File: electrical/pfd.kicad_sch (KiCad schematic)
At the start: 8 parts

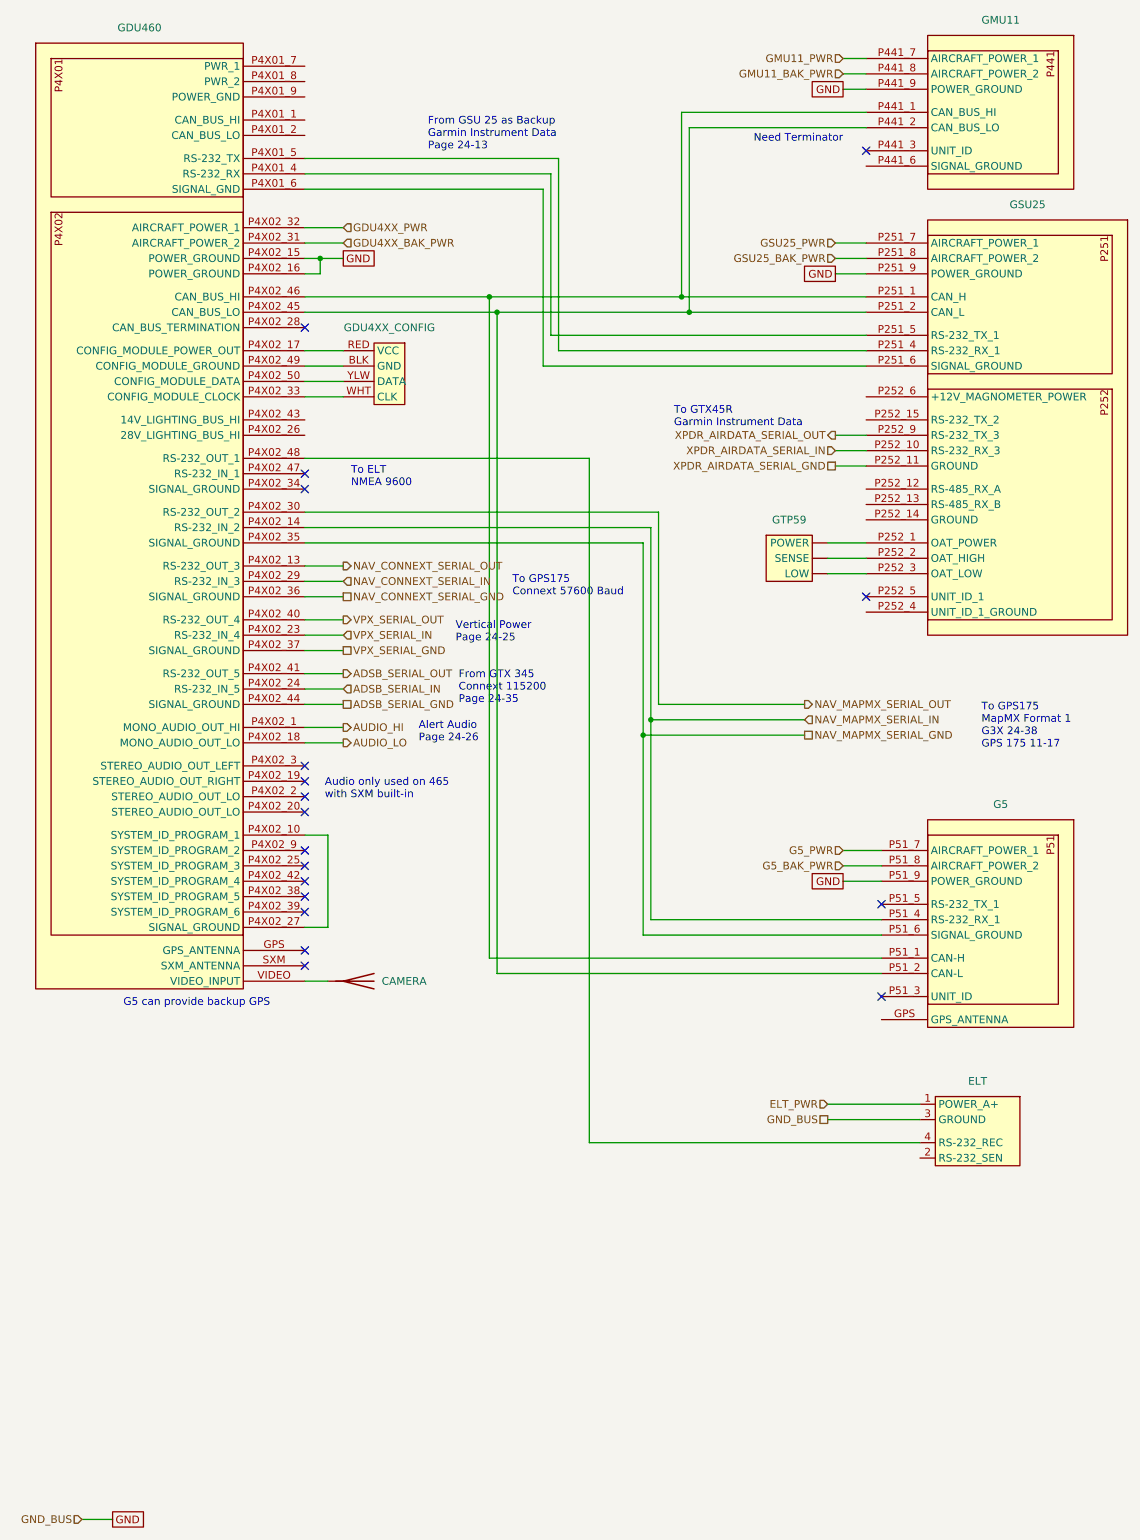
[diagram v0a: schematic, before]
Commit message: Changed GPS 175 to not have connection to GTS 205x per g3xpert. Moved ELT GPS from GPS 175 and used RS-232 on GDU 460 for GEA 24 backup.
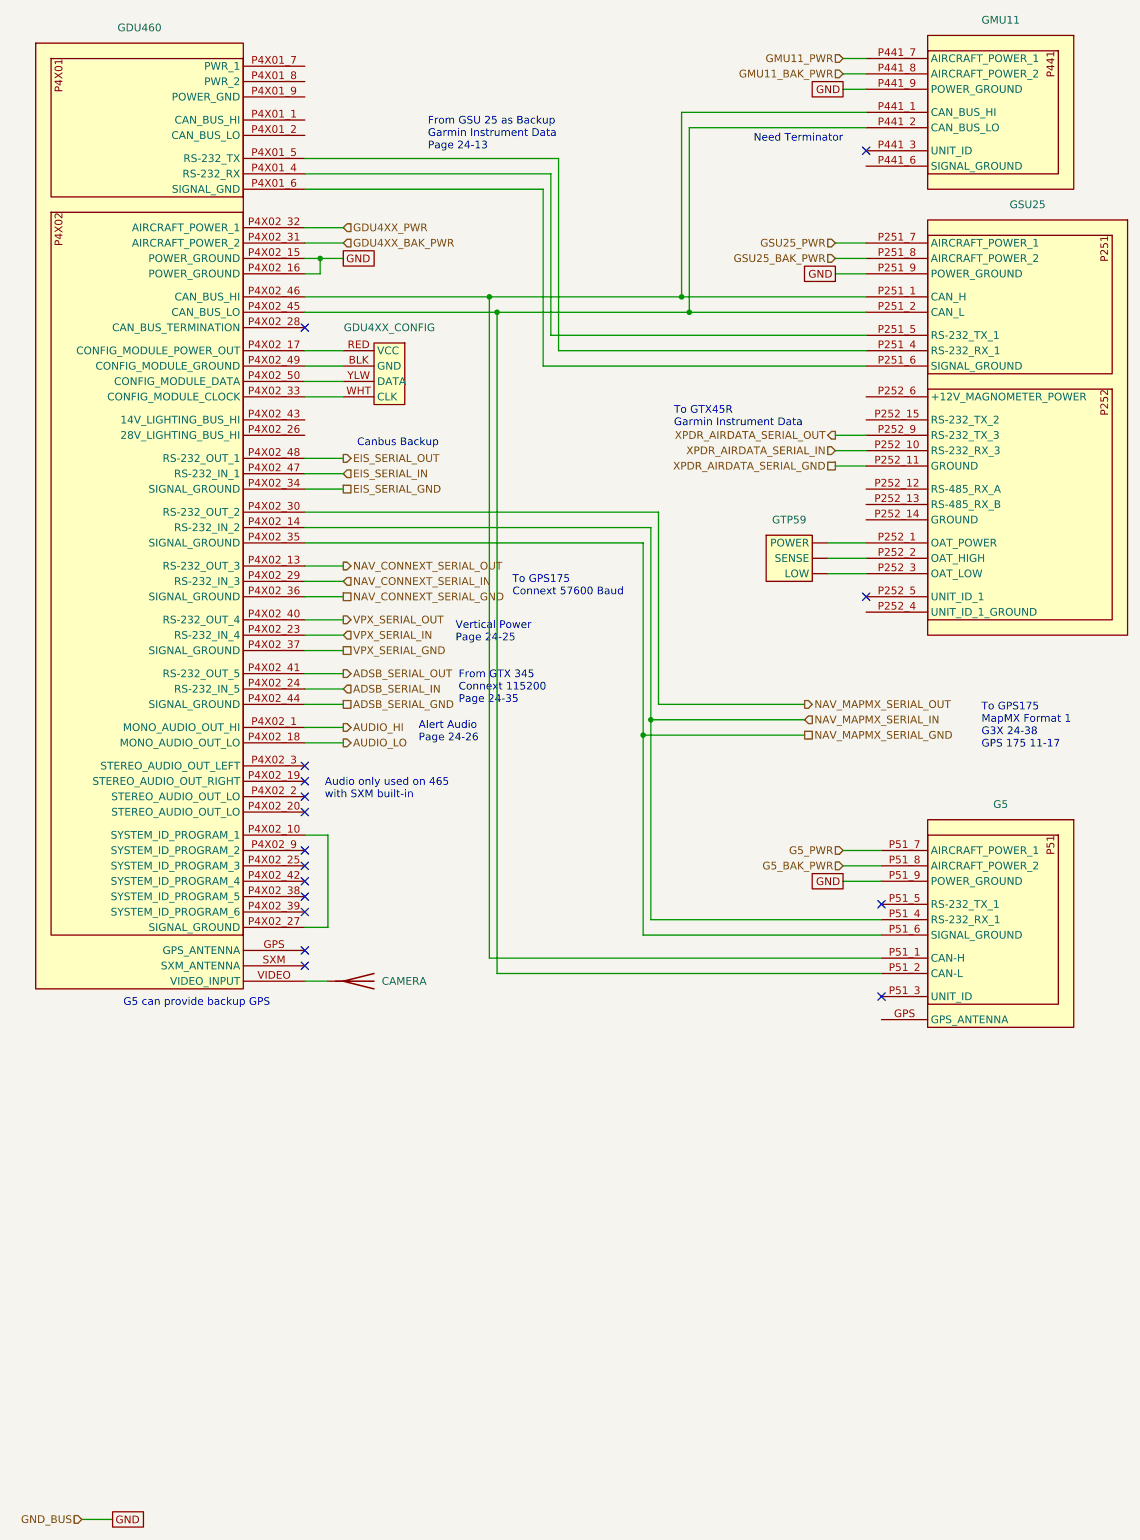
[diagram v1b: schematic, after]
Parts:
- removed ELT: ~, symbol flyerx:ACK_E-04
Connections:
- net EIS_SERIAL_GND: now reaches GDU460.P4X02_34 (SIGNAL_GROUND)
- net EIS_SERIAL_IN: now reaches GDU460.P4X02_47 (RS-232_IN_1)
- net EIS_SERIAL_OUT: now reaches GDU460.P4X02_48 (RS-232_OUT_1)
- no-connect marks 18 -> 16
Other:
- note added: "Canbus Backup"
- note removed: "To ELT NMEA 9600"
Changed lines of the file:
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@@
 	(title_block
 		(title "PFD & ADAHRS")
-		(date "2025-09-08")
-		(rev "1.0")
+		(date "2025-09-09")
+		(rev "1.0.1")
 		(company "N78HR")
 	)
@@
 		)
 	)
-	(text "To ELT\nNMEA 9600"
-		(exclude_from_sim no)
-		(at 69.85 91.186 0)
-		(effects
-			(font
-				(size 1.27 1.27)
-			)
-			(justify left bottom)
-		)
-	)
 	(text "Audio only used on 465\nwith SXM built-in"
 		(exclude_from_sim no)
@@
 			)
 			(justify left)
+		)
+	)
+	(text "Canbus Backup"
+		(exclude_from_sim no)
+		(at 70.866 84.582 0)
+		(effects
+			(font
+				(size 1.27 1.27)
+			)
+			(justify left bottom)
 		)
 	)
@@
 	)
 	(no_connect
-		(at 62.23 91.44)
-	)
-	(no_connect
 		(at 62.23 144.78)
 	)
@@
 	)
 	(no_connect
-		(at 62.23 88.9)
-	)
-	(no_connect
 		(at 62.23 137.16)
 	)
@@
 	(wire
 		(pts
-			(xy 109.22 86.36) (xy 109.22 199.39)
-		)
-		(stroke
-			(width 0)
-			(type default)
-		)
-	)
-	(wire
-		(pts
 			(xy 62.23 55.88) (xy 64.77 55.88)
 		)
@@
 	(wire
 		(pts
+			(xy 62.23 88.9) (xy 68.58 88.9)
+		)
+		(stroke
+			(width 0)
+			(type default)
+		)
+	)
+	(wire
+		(pts
 			(xy 124.46 59.69) (xy 154.94 59.69)
 		)
@@
 	(wire
 		(pts
-			(xy 109.22 199.39) (xy 163.83 199.39)
-		)
-		(stroke
-			(width 0)
-			(type default)
-		)
-	)
-	(wire
-		(pts
 			(xy 120.65 127) (xy 120.65 95.25)
 		)
@@
 	(wire
 		(pts
+			(xy 62.23 91.44) (xy 68.58 91.44)
+		)
+		(stroke
+			(width 0)
+			(type default)
+		)
+	)
+	(wire
+		(pts
 			(xy 151.13 151.13) (xy 157.48 151.13)
 		)
@@
 	(wire
 		(pts
+			(xy 62.23 86.36) (xy 68.58 86.36)
+		)
+		(stroke
+			(width 0)
+			(type default)
+		)
+	)
+	(wire
+		(pts
 			(xy 62.23 121.92) (xy 68.58 121.92)
 		)
@@
 	(wire
 		(pts
-			(xy 148.59 195.58) (xy 163.83 195.58)
-		)
-		(stroke
-			(width 0)
-			(type default)
-		)
-	)
-	(wire
-		(pts
 			(xy 62.23 172.72) (xy 66.04 172.72)
 		)
@@
 		(pts
 			(xy 62.23 148.59) (xy 66.04 148.59)
-		)
-		(stroke
-			(width 0)
-			(type default)
-		)
-	)
-	(wire
-		(pts
-			(xy 148.59 193.04) (xy 163.83 193.04)
-		)
-		(stroke
-			(width 0)
-			(type default)
-		)
-	)
-	(wire
-		(pts
-			(xy 62.23 86.36) (xy 109.22 86.36)
 		)
 		(stroke
@@
 		)
 	)
+	(hierarchical_label "EIS_SERIAL_OUT"
+		(shape output)
+		(at 68.58 86.36 0)
+		(effects
+			(font
+				(size 1.27 1.27)
+			)
+			(justify left)
+		)
+	)
 	(hierarchical_label "ADSB_SERIAL_GND"
 		(shape passive)
@@
 		)
 	)
+	(hierarchical_label "EIS_SERIAL_GND"
+		(shape passive)
+		(at 68.58 91.44 0)
+		(effects
+			(font
+				(size 1.27 1.27)
+			)
+			(justify left)
+		)
+	)
 	(hierarchical_label "VPX_SERIAL_OUT"
 		(shape output)
@@
 		)
 	)
-	(hierarchical_label "ELT_PWR"
-		(shape input)
-		(at 148.59 193.04 180)
-		(effects
-			(font
-				(size 1.27 1.27)
-			)
-			(justify right)
-		)
-	)
 	(hierarchical_label "GSU25_BAK_PWR"
 		(shape input)
@@
 		)
 	)
+	(hierarchical_label "EIS_SERIAL_IN"
+		(shape input)
+		(at 68.58 88.9 0)
+		(effects
+			(font
+				(size 1.27 1.27)
+			)
+			(justify left)
+		)
+	)
 	(hierarchical_label "NAV_CONNEXT_SERIAL_IN"
 		(shape input)
@@
 		(shape input)
 		(at 149.86 50.8 180)
-		(effects
-			(font
-				(size 1.27 1.27)
-			)
-			(justify right)
-		)
-	)
-	(hierarchical_label "GND_BUS"
-		(shape passive)
-		(at 148.59 195.58 180)
 		(effects
 			(font
@@
 					(unit 1)
 				)
-			)
-		)
-	)
-	(symbol
-		(lib_id "flyerx:ACK_E-04")
-		(at 180.34 191.77 0)
-		(mirror y)
-		(unit 1)
-		(exclude_from_sim no)
-		(in_bom yes)
-		(on_board yes)
-		(dnp no)
-		(property "Reference" "ELT"
-			(at 173.355 189.23 0)
-			(effects
-				(font
-					(size 1.27 1.27)
-				)
-			)
-		)
-		(property "Value" "~"
-			(at 180.34 190.5 0)
-			(effects
-				(font
-					(size 1.27 1.27)
-				)
-			)
-		)
-		(property "Footprint" ""
-			(at 180.34 190.5 0)
-			(effects
-				(font
-					(size 1.27 1.27)
-				)
-				(hide yes)
-			)
-		)
-		(property "Datasheet" ""
-			(at 180.34 190.5 0)
-			(effects
-				(font
-					(size 1.27 1.27)
-				)
-				(hide yes)
-			)
-		)
-		(property "Description" ""
-			(at 180.34 191.77 0)
-			(effects
-				(font
-					(size 1.27 1.27)
-				)
-			)
-		)
-		(pin "1"
-		)
-		(pin "2"
-		)
-		(pin "4"
-		)
-		(pin "3"
-		)
-		(instances
-			(project "electrical"
-				(path "/e8ec215a-dbe2-4eba-a577-e50a0a128049/633b5331-dc3f-449e-8212-24f89753723c"
-					(reference "ELT")
-					(unit 1)
-				)

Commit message: Rewired canbus to match physical order.
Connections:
- net CAN_G5_HI_OUT: now reaches G5.P51_1 (CAN-H), GDU460.P4X02_46 (CAN_BUS_HI), GSU25.P251_1 (CAN_H)
- net CAN_G5_HI_OUT: no longer GMU11.P441_1 (CAN_BUS_HI)
- net CAN_G5_LO_OUT: now reaches G5.P51_2 (CAN-L), GDU460.P4X02_45 (CAN_BUS_LO), GSU25.P251_2 (CAN_L)
- net CAN_G5_LO_OUT: no longer GMU11.P441_2 (CAN_BUS_LO)
- new net CAN_GMU_HI_IN: GMU11.P441_1 (CAN_BUS_HI)
- new net CAN_GMU_LO_IN: GMU11.P441_2 (CAN_BUS_LO)
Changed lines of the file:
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@@
 		(title "PFD & ADAHRS")
 		(date "2025-09-09")
-		(rev "1.0.1")
+		(rev "1.0.3")
 		(company "N78HR")
 	)
@@
 	(text "Need Terminator"
 		(exclude_from_sim no)
-		(at 151.13 34.29 0)
+		(at 150.114 35.306 0)
 		(effects
 			(font
@@
 			(justify left bottom)
 		)
-	)
-	(junction
-		(at 125.73 62.23)
-		(diameter 0)
-		(color 0 0 0 0)
 	)
 	(junction
@@
 	)
 	(junction
-		(at 124.46 59.69)
+		(at 152.4 168.91)
+		(diameter 0)
+		(color 0 0 0 0)
+	)
+	(junction
+		(at 143.51 59.69)
+		(diameter 0)
+		(color 0 0 0 0)
+	)
+	(junction
+		(at 153.67 171.45)
 		(diameter 0)
 		(color 0 0 0 0)
@@
 		(color 0 0 0 0)
 	)
+	(junction
+		(at 142.24 62.23)
+		(diameter 0)
+		(color 0 0 0 0)
+	)
 	(no_connect
 		(at 62.23 144.78)
@@
 	(wire
 		(pts
+			(xy 137.16 55.88) (xy 143.51 55.88)
+		)
+		(stroke
+			(width 0)
+			(type default)
+		)
+	)
+	(wire
+		(pts
 			(xy 149.86 50.8) (xy 154.94 50.8)
 		)
@@
 	(wire
 		(pts
-			(xy 124.46 59.69) (xy 154.94 59.69)
+			(xy 92.71 59.69) (xy 143.51 59.69)
 		)
 		(stroke
@@
 	(wire
 		(pts
+			(xy 152.4 168.91) (xy 157.48 168.91)
+		)
+		(stroke
+			(width 0)
+			(type default)
+		)
+	)
+	(wire
+		(pts
 			(xy 120.65 95.25) (xy 62.23 95.25)
 		)
@@
 	(wire
 		(pts
-			(xy 154.94 31.75) (xy 125.73 31.75)
-		)
-		(stroke
-			(width 0)
-			(type default)
-		)
-	)
-	(wire
-		(pts
 			(xy 66.04 148.59) (xy 66.04 163.83)
 		)
@@
 	(wire
 		(pts
+			(xy 153.67 176.53) (xy 153.67 171.45)
+		)
+		(stroke
+			(width 0)
+			(type default)
+		)
+	)
+	(wire
+		(pts
 			(xy 104.14 36.83) (xy 104.14 68.58)
 		)
@@
 	(wire
 		(pts
-			(xy 125.73 31.75) (xy 125.73 62.23)
-		)
-		(stroke
-			(width 0)
-			(type default)
-		)
-	)
-	(wire
-		(pts
 			(xy 149.86 87.63) (xy 154.94 87.63)
 		)
@@
 	(wire
 		(pts
+			(xy 137.16 58.42) (xy 142.24 58.42)
+		)
+		(stroke
+			(width 0)
+			(type default)
+		)
+	)
+	(wire
+		(pts
 			(xy 62.23 53.34) (xy 64.77 53.34)
 		)
@@
 	(wire
 		(pts
+			(xy 153.67 171.45) (xy 157.48 171.45)
+		)
+		(stroke
+			(width 0)
+			(type default)
+		)
+	)
+	(wire
+		(pts
 			(xy 151.13 151.13) (xy 157.48 151.13)
 		)
@@
 	(wire
 		(pts
-			(xy 93.98 171.45) (xy 157.48 171.45)
+			(xy 93.98 171.45) (xy 153.67 171.45)
 		)
 		(stroke
@@
 	(wire
 		(pts
+			(xy 151.13 31.75) (xy 154.94 31.75)
+		)
+		(stroke
+			(width 0)
+			(type default)
+		)
+	)
+	(wire
+		(pts
 			(xy 151.13 22.86) (xy 154.94 22.86)
 		)
@@
 	(wire
 		(pts
-			(xy 92.71 168.91) (xy 157.48 168.91)
+			(xy 92.71 168.91) (xy 152.4 168.91)
 		)
 		(stroke
@@
 	(wire
 		(pts
+			(xy 148.59 173.99) (xy 152.4 173.99)
+		)
+		(stroke
+			(width 0)
+			(type default)
+		)
+	)
+	(wire
+		(pts
 			(xy 101.6 41.91) (xy 62.23 41.91)
 		)
@@
 	(wire
 		(pts
+			(xy 142.24 58.42) (xy 142.24 62.23)
+		)
+		(stroke
+			(width 0)
+			(type default)
+		)
+	)
+	(wire
+		(pts
+			(xy 152.4 173.99) (xy 152.4 168.91)
+		)
+		(stroke
+			(width 0)
+			(type default)
+		)
+	)
+	(wire
+		(pts
 			(xy 151.13 20.32) (xy 154.94 20.32)
 		)
@@
 	(wire
 		(pts
+			(xy 148.59 176.53) (xy 153.67 176.53)
+		)
+		(stroke
+			(width 0)
+			(type default)
+		)
+	)
+	(wire
+		(pts
 			(xy 119.38 129.54) (xy 119.38 97.79)
 		)
@@
 	(wire
 		(pts
-			(xy 125.73 62.23) (xy 154.94 62.23)
+			(xy 93.98 62.23) (xy 142.24 62.23)
 		)
 		(stroke
@@
 	(wire
 		(pts
+			(xy 142.24 62.23) (xy 154.94 62.23)
+		)
+		(stroke
+			(width 0)
+			(type default)
+		)
+	)
+	(wire
+		(pts
 			(xy 62.23 106.68) (xy 68.58 106.68)
 		)
@@
 	(wire
 		(pts
-			(xy 93.98 62.23) (xy 125.73 62.23)
-		)
-		(stroke
-			(width 0)
-			(type default)
-		)
-	)
-	(wire
-		(pts
 			(xy 93.98 62.23) (xy 93.98 171.45)
 		)
@@
 	(wire
 		(pts
-			(xy 154.94 29.21) (xy 124.46 29.21)
+			(xy 143.51 55.88) (xy 143.51 59.69)
 		)
 		(stroke
@@
 	(wire
 		(pts
-			(xy 92.71 59.69) (xy 124.46 59.69)
+			(xy 143.51 59.69) (xy 154.94 59.69)
 		)
 		(stroke
@@
 	(wire
 		(pts
+			(xy 151.13 29.21) (xy 154.94 29.21)
+		)
+		(stroke
+			(width 0)
+			(type default)
+		)
+	)
+	(wire
+		(pts
 			(xy 62.23 148.59) (xy 66.04 148.59)
 		)
@@
 		(pts
 			(xy 66.04 163.83) (xy 62.23 163.83)
-		)
-		(stroke
-			(width 0)
-			(type default)
-		)
-	)
-	(wire
-		(pts
-			(xy 124.46 29.21) (xy 124.46 59.69)
 		)
 		(stroke
@@
 		)
 	)
+	(hierarchical_label "CAN_GMU_HI_IN"
+		(shape input)
+		(at 151.13 29.21 180)
+		(effects
+			(font
+				(size 1.27 1.27)
+			)
+			(justify right)
+		)
+	)
 	(hierarchical_label "XPDR_AIRDATA_SERIAL_OUT"
 		(shape output)
@@
 		)
 	)
+	(hierarchical_label "CAN_GSU_LO_IN"
+		(shape input)
+		(at 137.16 58.42 180)
+		(effects
+			(font
+				(size 1.27 1.27)
+			)
+			(justify right)
+		)
+	)
 	(hierarchical_label "AUDIO_HI"
 		(shape output)
@@
 		)
 	)
+	(hierarchical_label "CAN_GMU_LO_IN"
+		(shape input)
+		(at 151.13 31.75 180)
+		(effects
+			(font
+				(size 1.27 1.27)
+			)
+			(justify right)
+		)
+	)
+	(hierarchical_label "CAN_GSU_HI_IN"
+		(shape input)
+		(at 137.16 55.88 180)
+		(effects
+			(font
+				(size 1.27 1.27)
+			)
+			(justify right)
+		)
+	)
 	(hierarchical_label "ADSB_SERIAL_OUT"
 		(shape output)
@@
 		(effects
 			(font
+				(size 1.27 1.27)
+			)
+			(justify right)
+		)
+	)
+	(hierarchical_label "CAN_G5_HI_OUT"
+		(shape output)
+		(at 148.59 173.99 180)
+		(effects
+			(font
+				(size 1.27 1.27)
+			)
+			(justify right)
+		)
+	)
+	(hierarchical_label "CAN_G5_LO_OUT"
+		(shape output)
+		(at 148.59 176.53 180)
+		(effects
+			(font

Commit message: Added RS232 and Canbus wiring notation
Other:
- note added: "Connector Shield"
- note added: "Destination Connector Shield"
- note added: "Source Connector Shield"
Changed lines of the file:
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@@
 	(title_block
 		(title "PFD & ADAHRS")
-		(date "2025-09-09")
-		(rev "1.0.3")
+		(date "2025-10-02")
+		(rev "1.1.4")
 		(company "N78HR")
+	)
+	(text "Source\nConnector Shield"
+		(exclude_from_sim no)
+		(at 108.966 126.492 0)
+		(effects
+			(font
+				(size 1.27 1.27)
+			)
+		)
+	)
+	(text "Connector Shield"
+		(exclude_from_sim no)
+		(at 102.87 135.128 0)
+		(effects
+			(font
+				(size 1.27 1.27)
+			)
+		)
+	)
+	(text "Source\nConnector Shield"
+		(exclude_from_sim no)
+		(at 110.744 114.808 0)
+		(effects
+			(font
+				(size 1.27 1.27)
+			)
+		)
+	)
+	(text "Source\nConnector Shield"
+		(exclude_from_sim no)
+		(at 102.616 88.392 0)
+		(effects
+			(font
+				(size 1.27 1.27)
+			)
+		)
+	)
+	(text "Destination\nConnector Shield"
+		(exclude_from_sim no)
+		(at 146.05 74.422 0)
+		(effects
+			(font
+				(size 1.27 1.27)
+			)
+		)
 	)
 	(text "Vertical Power\nPage 24-25"
@@
 		)
 	)
+	(text "Source\nConnector Shield"
+		(exclude_from_sim no)
+		(at 70.612 34.036 0)
+		(effects
+			(font
+				(size 1.27 1.27)
+			)
+		)
+	)
 	(text "To GPS175\nMapMX Format 1\nG3X 24-38\nGPS 175 11-17"
 		(exclude_from_sim no)
@@
 			)
 			(justify left bottom)
+		)
+	)
+	(text "Source\nConnector Shield"
+		(exclude_from_sim no)
+		(at 132.334 91.44 0)
+		(effects
+			(font
+				(size 1.27 1.27)
+			)
 		)
 	)
@@
 		)
 	)
+	(text "Source\nConnector Shield"
+		(exclude_from_sim no)
+		(at 107.696 102.362 0)
+		(effects
+			(font
+				(size 1.27 1.27)
+			)
+		)
+	)

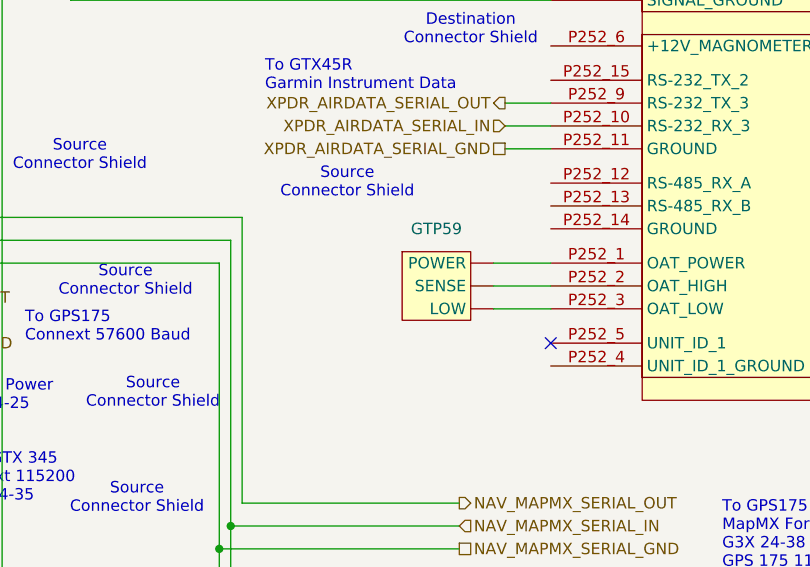
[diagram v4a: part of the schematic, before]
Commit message: Added connector for GTP 59.
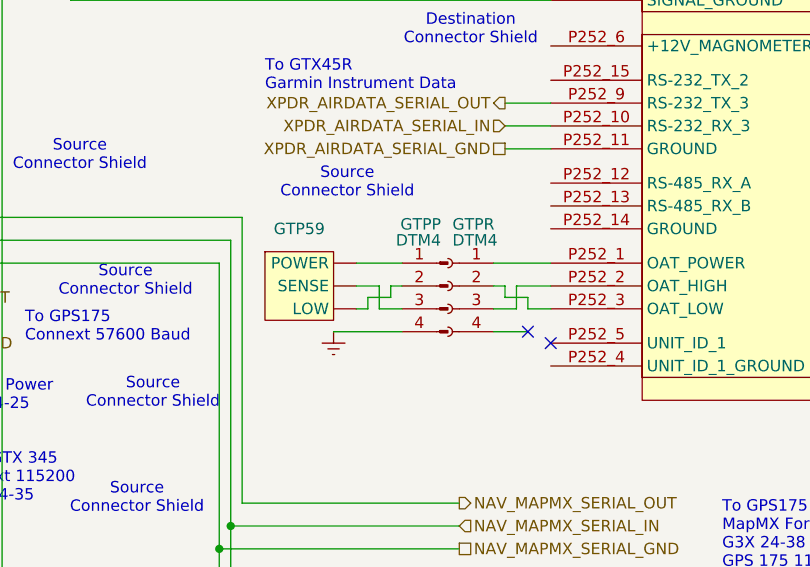
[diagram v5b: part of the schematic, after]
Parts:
- added GTPP: DTM4, symbol Connector:Conn_01x04_Pin
- added GTPR: DTM4, symbol Connector:Conn_01x04_Socket
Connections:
- net at GTP59. (LOW): now also GTPP.3 (Pin_3); no longer GSU25.P252_1 (OAT_POWER)
- net at GSU25.P252_2 (OAT_HIGH): now also GTPR.3 (Pin_3); no longer GTP59. (LOW)
- net at GSU25.P252_3 (OAT_LOW): now also GTPR.2 (Pin_2); no longer GTP59. (LOW)
- new net: GTP59. (LOW), GTPP.1 (Pin_1)
- new net: GTP59. (LOW), GTPP.2 (Pin_2)
- new net: GSU25.P252_1 (OAT_POWER), GTPR.1 (Pin_1)
- new net Earth: GTPP.4 (Pin_4)
- no-connect marks 16 -> 17
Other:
- moved on the sheet: GTP59

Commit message: Added colors to GTP 59 symbol. Moved power around as best as I could to accomodate lights together.
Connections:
- net at GTPP.1 (Pin_1): now also GTP59.W (POWER); no longer GTP59. (LOW)
- net at GTPP.2 (Pin_2): now also GTP59.O (LOW); no longer GTP59. (LOW)
- net at GTPP.3 (Pin_3): now also GTP59.B (SENSE); no longer GTP59. (LOW)
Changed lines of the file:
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@@
 	(title_block
 		(title "PFD & ADAHRS")
-		(date "2025-10-03")
-		(rev "1.1.5")
+		(date "2025-10-12")
+		(rev "1.1.8")
 		(company "N78HR")
 	)
@@
 			)
 		)
-		(pin ""
-		)
-		(pin ""
-		)
-		(pin ""
+		(pin "O"
+		)
+		(pin "B"
+		)
+		(pin "W"
 		)
 		(instances
